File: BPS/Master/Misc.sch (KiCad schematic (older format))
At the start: 20 parts, among them J14 Conn_01x18, J3 FrontFans, J4 BackFans, Q6 BUT11

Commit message: Assigned footprints to all symbols except reset circuit(high voltage detector). Changed 18 pin connector to 3, 6 pin connectors. Generated netlist.
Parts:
- removed J14: Conn_01x18, symbol Connector_Generic:Conn_01x18
- added J12, J14, J15: Conn_01x06, UTSVT_Connectors:Molex_MicroFit_01x06_Horizontal, symbol Connector_Generic:Conn_01x06
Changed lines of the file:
@@
 Entry Wire Line
 	5300 4600 5400 4700
-$Comp
-L Connector_Generic:Conn_01x18 J14
-U 1 1 5F0A4204
-P 3700 6000
-F 0 "J14" V 3825 5946 50  0000 C CNN
-F 1 "Conn_01x18" V 3916 5946 50  0000 C CNN
-F 2 "" H 3700 6000 50  0001 C CNN
-F 3 "~" H 3700 6000 50  0001 C CNN
-	1    3700 6000
-	0    1    1    0
-$EndComp
 Wire Wire Line
 	2000 4700 2000 5800
@@
 Text Label 5400 4700 3    50   ~ 0
 IP17
+$Comp
+L Connector_Generic:Conn_01x06 J12
+U 1 1 5EF7E85A
+P 3100 6000
+F 0 "J12" V 3300 5950 50  0000 L CNN
+F 1 "Conn_01x06" V 3200 5750 50  0000 L CNN
+F 2 "UTSVT_Connectors:Molex_MicroFit_01x06_Horizontal" H 3100 6000 50  0001 C CNN
+F 3 "~" H 3100 6000 50  0001 C CNN
+	1    3100 6000
+	0    1    1    0
+$EndComp
+$Comp
+L Connector_Generic:Conn_01x06 J14
+U 1 1 5EF7ED81
+P 3700 6000
+F 0 "J14" V 3900 5900 50  0000 L CNN
+F 1 "Conn_01x06" V 3800 5750 50  0000 L CNN
+F 2 "UTSVT_Connectors:Molex_MicroFit_01x06_Horizontal" H 3700 6000 50  0001 C CNN
+F 3 "~" H 3700 6000 50  0001 C CNN
+	1    3700 6000
+	0    1    1    0
+$EndComp
+$Comp
+L Connector_Generic:Conn_01x06 J15
+U 1 1 5EF50D99
+P 4300 6000
+F 0 "J15" V 4500 5950 50  0000 L CNN
+F 1 "Conn_01x06" V 4400 5750 50  0000 L CNN
+F 2 "UTSVT_Connectors:Molex_MicroFit_01x06_Horizontal" H 4300 6000 50  0001 C CNN
+F 3 "~" H 4300 6000 50  0001 C CNN
+	1    4300 6000
+	0    1    1    0
+$EndComp
 Wire Bus Line
 	4350 1500 5450 1500

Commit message: Made file paths of symbol libraries relative. Added footprint for high voltage detection that is SMD and has same specs as one recommended in Bluetooth Module datasheet.
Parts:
- removed J12, J14, J15: Conn_01x06, UTSVT_Connectors:Molex_MicroFit_01x06_Horizontal, symbol Connector_Generic:Conn_01x06
- added J12, J14: Conn_01x08, UTSVT_Connectors:Molex_MicroFit3.0_2x4xP3.00mm_PolarizingPeg_Vertical, symbol Connector_Generic:Conn_01x08
- added J15: Conn_01x02, UTSVT_Connectors:Molex_MicroFit3.0_1x2xP3.00mm_PolarizingPeg_Vertical, symbol Connector_Generic:Conn_01x02
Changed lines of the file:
@@
 Text Label 5400 4700 3    50   ~ 0
 IP17
-$Comp
-L Connector_Generic:Conn_01x06 J12
-U 1 1 5EF7E85A
-P 3100 6000
-F 0 "J12" V 3300 5950 50  0000 L CNN
-F 1 "Conn_01x06" V 3200 5750 50  0000 L CNN
-F 2 "UTSVT_Connectors:Molex_MicroFit_01x06_Horizontal" H 3100 6000 50  0001 C CNN
-F 3 "~" H 3100 6000 50  0001 C CNN
-	1    3100 6000
-	0    1    1    0
-$EndComp
-$Comp
-L Connector_Generic:Conn_01x06 J14
-U 1 1 5EF7ED81
-P 3700 6000
-F 0 "J14" V 3900 5900 50  0000 L CNN
-F 1 "Conn_01x06" V 3800 5750 50  0000 L CNN
-F 2 "UTSVT_Connectors:Molex_MicroFit_01x06_Horizontal" H 3700 6000 50  0001 C CNN
-F 3 "~" H 3700 6000 50  0001 C CNN
-	1    3700 6000
-	0    1    1    0
-$EndComp
-$Comp
-L Connector_Generic:Conn_01x06 J15
-U 1 1 5EF50D99
-P 4300 6000
-F 0 "J15" V 4500 5950 50  0000 L CNN
-F 1 "Conn_01x06" V 4400 5750 50  0000 L CNN
-F 2 "UTSVT_Connectors:Molex_MicroFit_01x06_Horizontal" H 4300 6000 50  0001 C CNN
-F 3 "~" H 4300 6000 50  0001 C CNN
-	1    4300 6000
-	0    1    1    0
-$EndComp
 Wire Bus Line
 	4350 1500 5450 1500
@@
 Wire Bus Line
 	1800 4600 5500 4600
+$Comp
+L Connector_Generic:Conn_01x08 J12
+U 1 1 5EF670FD
+P 3200 6000
+F 0 "J12" V 3400 5950 50  0000 L CNN
+F 1 "Conn_01x08" V 3300 5750 50  0000 L CNN
+F 2 "UTSVT_Connectors:Molex_MicroFit3.0_2x4xP3.00mm_PolarizingPeg_Vertical" H 3200 6000 50  0001 C CNN
+F 3 "~" H 3200 6000 50  0001 C CNN
+	1    3200 6000
+	0    1    1    0
+$EndComp
+$Comp
+L Connector_Generic:Conn_01x08 J14
+U 1 1 5EF67B62
+P 4000 6000
+F 0 "J14" V 4200 5950 50  0000 L CNN
+F 1 "Conn_01x08" V 4100 5750 50  0000 L CNN
+F 2 "UTSVT_Connectors:Molex_MicroFit3.0_2x4xP3.00mm_PolarizingPeg_Vertical" H 4000 6000 50  0001 C CNN
+F 3 "~" H 4000 6000 50  0001 C CNN
+	1    4000 6000
+	0    1    1    0
+$EndComp
+$Comp
+L Connector_Generic:Conn_01x02 J15
+U 1 1 5EF68778
+P 4500 6000
+F 0 "J15" V 4700 5900 50  0000 L CNN
+F 1 "Conn_01x02" V 4600 5750 50  0000 L CNN
+F 2 "UTSVT_Connectors:Molex_MicroFit3.0_1x2xP3.00mm_PolarizingPeg_Vertical" H 4500 6000 50  0001 C CNN
+F 3 "~" H 4500 6000 50  0001 C CNN
+	1    4500 6000
+	0    1    1    0
+$EndComp
 $EndSCHEMATC

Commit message: Created new board for Bluetooth module because the antenna cannot have a ground plane on it. Made everything connect using pin headers. Will mount the Bluetooth module board onto the Master board.
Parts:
- removed J12, J14: Conn_01x08, UTSVT_Connectors:Molex_MicroFit3.0_2x4xP3.00mm_PolarizingPeg_Vertical, symbol Connector_Generic:Conn_01x08
- removed J15: Conn_01x02, UTSVT_Connectors:Molex_MicroFit3.0_1x2xP3.00mm_PolarizingPeg_Vertical, symbol Connector_Generic:Conn_01x02
- added J12, J14, J15: Conn_01x06, Connector_PinHeader_2.54mm:PinHeader_1x06_P2.54mm_Vertical, symbol Connector_Generic:Conn_01x06
- added J?: Conn_01x04, symbol Connector_Generic:Conn_01x04
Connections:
- net labels added: USART1_CTS, USART1_RTS, USART1_RX, USART1_TX
- net labels removed: +12V
- wire segments 114 -> 122
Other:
- note added: "For Bluetooth Module"
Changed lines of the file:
@@
 FANPWR
-$Comp
-L power:+12V #PWR0118
-U 1 1 5EE38D3D
-P 7000 1050
-F 0 "#PWR0118" H 7000 900 50  0001 C CNN
-F 1 "+12V" H 7015 1223 50  0000 C CNN
-F 2 "" H 7000 1050 50  0001 C CNN
-F 3 "" H 7000 1050 50  0001 C CNN
-	1    7000 1050
-	1    0    0    -1
-$EndComp
 $Comp
 L Transistor_BJT:BUT11 Q6
@@
 Text Label 5400 4700 3    50   ~ 0
 IP17
+$Comp
+L power:GND #PWR0108
+U 1 1 5EF8895A
+P 7000 1050
+F 0 "#PWR0108" H 7000 800 50  0001 C CNN
+F 1 "GND" H 7005 877 50  0000 C CNN
+F 2 "" H 7000 1050 50  0001 C CNN
+F 3 "" H 7000 1050 50  0001 C CNN
+	1    7000 1050
+	-1   0    0    1
+$EndComp
+$Comp
+L Connector_Generic:Conn_01x06 J12
+U 1 1 5EF8DB7E
+P 3100 6000
+F 0 "J12" V 3300 5950 50  0000 L CNN
+F 1 "Conn_01x06" V 3200 5750 50  0000 L CNN
+F 2 "Connector_PinHeader_2.54mm:PinHeader_1x06_P2.54mm_Vertical" H 3100 6000 50  0001 C CNN
+F 3 "~" H 3100 6000 50  0001 C CNN
+	1    3100 6000
+	0    1    1    0
+$EndComp
+$Comp
+L Connector_Generic:Conn_01x06 J14
+U 1 1 5EF8E106
+P 3700 6000
+F 0 "J14" V 3900 5950 50  0000 L CNN
+F 1 "Conn_01x06" V 3800 5750 50  0000 L CNN
+F 2 "Connector_PinHeader_2.54mm:PinHeader_1x06_P2.54mm_Vertical" H 3700 6000 50  0001 C CNN
+F 3 "~" H 3700 6000 50  0001 C CNN
+	1    3700 6000
+	0    1    1    0
+$EndComp
+$Comp
+L Connector_Generic:Conn_01x06 J15
+U 1 1 5EF8EC17
+P 4300 6000
+F 0 "J15" V 4500 5950 50  0000 L CNN
+F 1 "Conn_01x06" V 4400 5750 50  0000 L CNN
+F 2 "Connector_PinHeader_2.54mm:PinHeader_1x06_P2.54mm_Vertical" H 4300 6000 50  0001 C CNN
+F 3 "~" H 4300 6000 50  0001 C CNN
+	1    4300 6000
+	0    1    1    0
+$EndComp
+Entry Wire Line
+	5500 4600 5600 4700
+Entry Wire Line
+	5700 4600 5800 4700
+Entry Wire Line
+	5900 4600 6000 4700
+Entry Wire Line
+	6100 4600 6200 4700
+$Comp
+L Connector_Generic:Conn_01x04 J?
+U 1 1 5EFCE394
+P 5950 6000
+F 0 "J?" V 5822 6180 50  0000 L CNN
+F 1 "Conn_01x04" V 5913 6180 50  0000 L CNN
+F 2 "" H 5950 6000 50  0001 C CNN
+F 3 "~" H 5950 6000 50  0001 C CNN
+	1    5950 6000
+	0    1    1    0
+$EndComp
+Text Notes 5500 6200 0    50   ~ 0
+For Bluetooth Module
+Wire Wire Line
+	5600 4700 5600 5800
+Wire Wire Line
+	5600 5800 5750 5800
+Wire Wire Line
+	5800 4700 5800 5800
+Wire Wire Line
+	5800 5800 5850 5800
+Wire Wire Line
+	6000 4700 6000 5800
+Wire Wire Line
+	6000 5800 5950 5800
+Wire Wire Line
+	6200 4700 6200 5800
+Wire Wire Line
+	6200 5800 6050 5800
 Wire Bus Line
 	4350 1500 5450 1500
@@
 	1050 1500 3750 1500
 Wire Bus Line
-	1800 4600 5500 4600
-$Comp
-L Connector_Generic:Conn_01x08 J12
-U 1 1 5EF670FD
-P 3200 6000
-F 0 "J12" V 3400 5950 50  0000 L CNN
-F 1 "Conn_01x08" V 3300 5750 50  0000 L CNN
-F 2 "UTSVT_Connectors:Molex_MicroFit3.0_2x4xP3.00mm_PolarizingPeg_Vertical" H 3200 6000 50  0001 C CNN
-F 3 "~" H 3200 6000 50  0001 C CNN
-	1    3200 6000
-	0    1    1    0
-$EndComp
-$Comp
-L Connector_Generic:Conn_01x08 J14
-U 1 1 5EF67B62
-P 4000 6000
-F 0 "J14" V 4200 5950 50  0000 L CNN
-F 1 "Conn_01x08" V 4100 5750 50  0000 L CNN
-F 2 "UTSVT_Connectors:Molex_MicroFit3.0_2x4xP3.00mm_PolarizingPeg_Vertical" H 4000 6000 50  0001 C CNN
-F 3 "~" H 4000 6000 50  0001 C CNN
-	1    4000 6000
-	0    1    1    0
-$EndComp
-$Comp
-L Connector_Generic:Conn_01x02 J15
-U 1 1 5EF68778
-P 4500 6000
-F 0 "J15" V 4700 5900 50  0000 L CNN
-F 1 "Conn_01x02" V 4600 5750 50  0000 L CNN
-F 2 "UTSVT_Connectors:Molex_MicroFit3.0_1x2xP3.00mm_PolarizingPeg_Vertical" H 4500 6000 50  0001 C CNN
-F 3 "~" H 4500 6000 50  0001 C CNN
-	1    4500 6000
-	0    1    1    0
-$EndComp
+	1800 4600 6300 4600
+Text Label 5600 4700 3    50   ~ 0
+USART1_TX
+Text Label 5800 4700 3    50   ~ 0
+USART1_RX
+Text Label 6000 4700 3    50   ~ 0
+USART1_CTS
+Text Label 6200 4700 3    50   ~ 0
+USART1_RTS
 $EndSCHEMATC

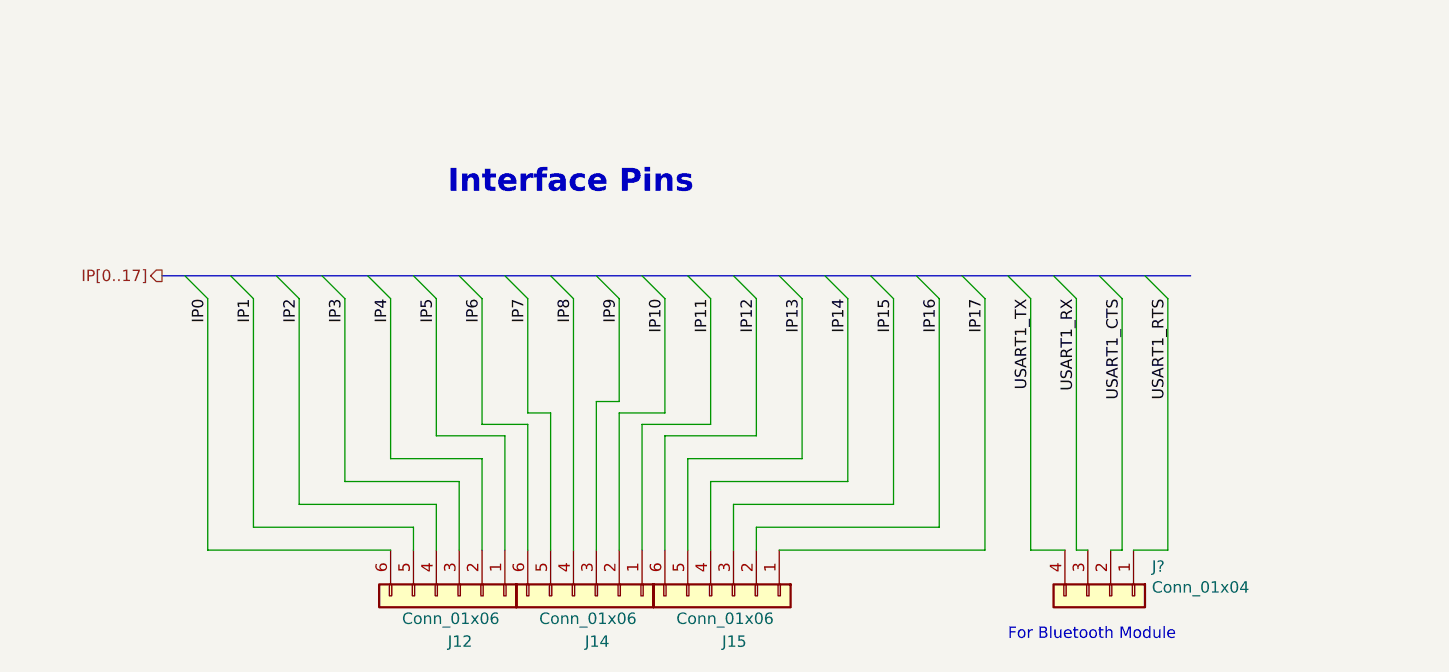
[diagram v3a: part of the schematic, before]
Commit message: Finished adding interface pins to master board. For some reason, the mosfet track isn't letting me connect to the fan power. I'm not sure why all these schematics are listed as modified because I didn't change anything in them.
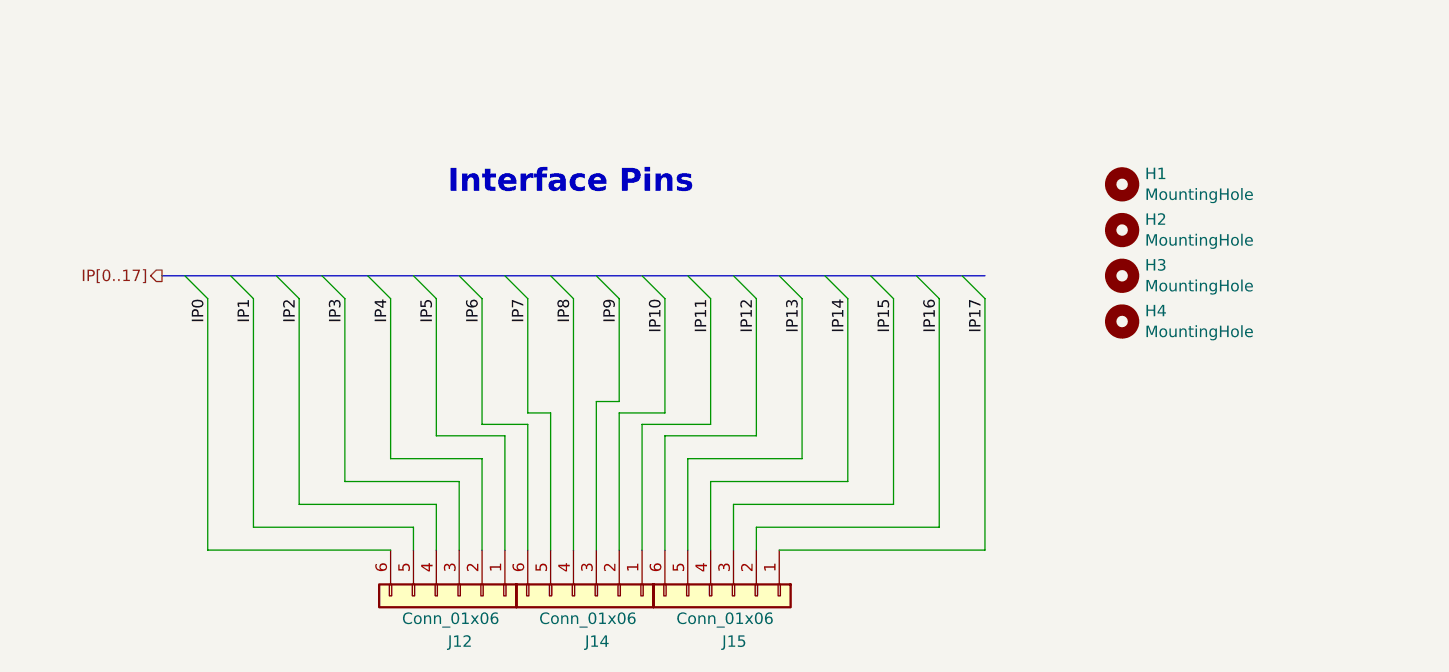
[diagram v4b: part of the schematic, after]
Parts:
- removed J?: Conn_01x04, symbol Connector_Generic:Conn_01x04
- added H1, H2, H3, H4: MountingHole, MountingHole:MountingHole_2.1mm, symbol Mechanical:MountingHole
- Q6: footprint Package_TO_SOT_THT:TO-220-3_Vertical -> Package_TO_SOT_SMD:SOT-23
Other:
- note removed: "For Bluetooth Module"
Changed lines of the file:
@@
 $Descr A4 11693 8268
 encoding utf-8
-Sheet 4 11
+Sheet 4 10
 Title ""
 Date ""
@@
 F 0 "Q6" H 7092 1296 50  0000 L CNN
 F 1 "BUT11" H 7092 1205 50  0000 L CNN
-F 2 "Package_TO_SOT_THT:TO-220-3_Vertical" H 7100 1175 50  0001 L CIN
+F 2 "Package_TO_SOT_SMD:SOT-23" H 7100 1175 50  0001 L CIN
 F 3 "http://www.fairchildsemi.com/ds/BU/BUT11.pdf" H 6900 1250 50  0001 L CNN
 	1    6900 1250
@@
 	0    1    1    0
 $EndComp
-Entry Wire Line
-	5500 4600 5600 4700
-Entry Wire Line
-	5700 4600 5800 4700
-Entry Wire Line
-	5900 4600 6000 4700
-Entry Wire Line
-	6100 4600 6200 4700
-$Comp
-L Connector_Generic:Conn_01x04 J?
-U 1 1 5EFCE394
-P 5950 6000
-F 0 "J?" V 5822 6180 50  0000 L CNN
-F 1 "Conn_01x04" V 5913 6180 50  0000 L CNN
-F 2 "" H 5950 6000 50  0001 C CNN
-F 3 "~" H 5950 6000 50  0001 C CNN
-	1    5950 6000
-	0    1    1    0
-$EndComp
-Text Notes 5500 6200 0    50   ~ 0
-For Bluetooth Module
-Wire Wire Line
-	5600 4700 5600 5800
-Wire Wire Line
-	5600 5800 5750 5800
-Wire Wire Line
-	5800 4700 5800 5800
-Wire Wire Line
-	5800 5800 5850 5800
-Wire Wire Line
-	6000 4700 6000 5800
-Wire Wire Line
-	6000 5800 5950 5800
-Wire Wire Line
-	6200 4700 6200 5800
-Wire Wire Line
-	6200 5800 6050 5800
+$Comp
+L Mechanical:MountingHole H?
+U 1 1 5F1A8D62
+P 6000 4800
+AR Path="/5F1A8D62" Ref="H?"  Part="1"
+AR Path="/5C392C6A/5F1A8D62" Ref="H4"  Part="1"
+F 0 "H4" H 6100 4846 50  0000 L CNN
+F 1 "MountingHole" H 6100 4755 50  0000 L CNN
+F 2 "MountingHole:MountingHole_2.1mm" H 6000 4800 50  0001 C CNN
+F 3 "~" H 6000 4800 50  0001 C CNN
+	1    6000 4800
+	1    0    0    -1
+$EndComp
+$Comp
+L Mechanical:MountingHole H?
+U 1 1 5F1A8D68
+P 6000 4600
+AR Path="/5F1A8D68" Ref="H?"  Part="1"
+AR Path="/5C392C6A/5F1A8D68" Ref="H3"  Part="1"
+F 0 "H3" H 6100 4646 50  0000 L CNN
+F 1 "MountingHole" H 6100 4555 50  0000 L CNN
+F 2 "MountingHole:MountingHole_2.1mm" H 6000 4600 50  0001 C CNN
+F 3 "~" H 6000 4600 50  0001 C CNN
+	1    6000 4600
+	1    0    0    -1
+$EndComp
+$Comp
+L Mechanical:MountingHole H?
+U 1 1 5F1A8D6E
+P 6000 4400
+AR Path="/5F1A8D6E" Ref="H?"  Part="1"
+AR Path="/5C392C6A/5F1A8D6E" Ref="H2"  Part="1"
+F 0 "H2" H 6100 4446 50  0000 L CNN
+F 1 "MountingHole" H 6100 4355 50  0000 L CNN
+F 2 "MountingHole:MountingHole_2.1mm" H 6000 4400 50  0001 C CNN
+F 3 "~" H 6000 4400 50  0001 C CNN
+	1    6000 4400
+	1    0    0    -1
+$EndComp
+$Comp
+L Mechanical:MountingHole H?
+U 1 1 5F1A8D74
+P 6000 4200
+AR Path="/5F1A8D74" Ref="H?"  Part="1"
+AR Path="/5C392C6A/5F1A8D74" Ref="H1"  Part="1"
+F 0 "H1" H 6100 4246 50  0000 L CNN
+F 1 "MountingHole" H 6100 4155 50  0000 L CNN
+F 2 "MountingHole:MountingHole_2.1mm" H 6000 4200 50  0001 C CNN
+F 3 "~" H 6000 4200 50  0001 C CNN
+	1    6000 4200
+	1    0    0    -1
+$EndComp
 Wire Bus Line
 	4350 1500 5450 1500
@@
 	1050 1500 3750 1500
 Wire Bus Line
-	1800 4600 6300 4600
-Text Label 5600 4700 3    50   ~ 0
-USART1_TX
-Text Label 5800 4700 3    50   ~ 0
-USART1_RX
-Text Label 6000 4700 3    50   ~ 0
-USART1_CTS
-Text Label 6200 4700 3    50   ~ 0
-USART1_RTS
+	1800 4600 5400 4600
 $EndSCHEMATC

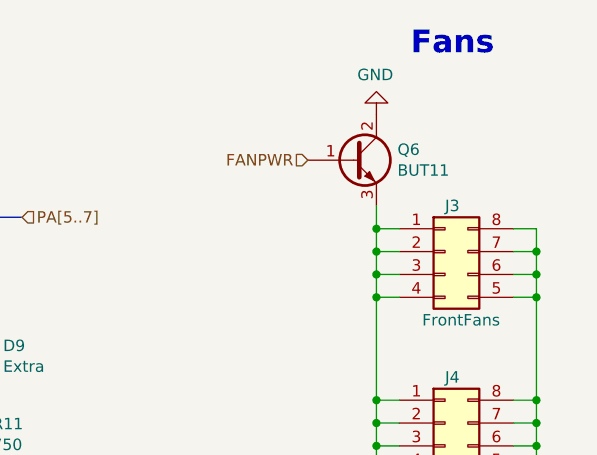
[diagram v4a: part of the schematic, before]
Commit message: Finished master board. Working to make sure that bluetooth mount won't cover anything important on master board, yet still be big enough to hold everything.
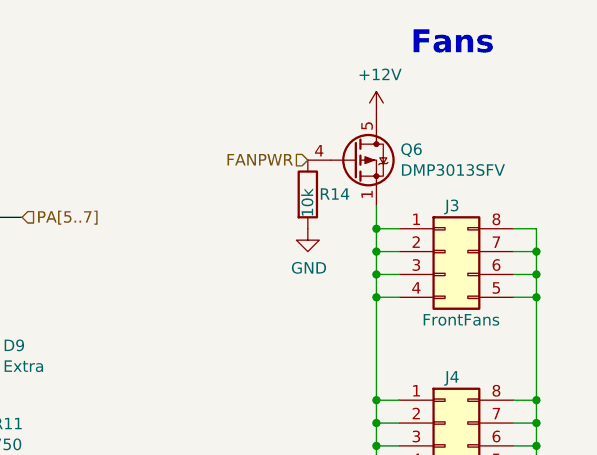
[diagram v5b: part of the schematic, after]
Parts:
- removed Q6: BUT11, Package_TO_SOT_SMD:SOT-23, symbol Transistor_BJT:BUT11
- added Q6: DMP3013SFV, Package_SON:Diodes_PowerDI3333-8, symbol Transistor_FET:DMP3013SFV
- added R14: 10k, Resistor_SMD:R_0805_2012Metric, symbol Device:R
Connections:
- net FANPWR: now also Q6.4 (G), R14.1
- net GND: now also R14.2
- net at J3.1 (Pin_1), J3.2 (Pin_2), J3.3 (Pin_3)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: now also Q6.1 (S), Q6.2 (S), Q6.3 (S)
- new net +12V: Q6.5 (D)
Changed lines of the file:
@@
 $EndComp
-Wire Wire Line
-	7000 1450 7000 1550
 Wire Wire Line
 	7000 1650 7100 1650
@@
 Connection ~ 7000 2500
 $Comp
-L power:GNDPWR #PWR030
-U 1 1 5C82C789
-P 7700 2700
-F 0 "#PWR030" H 7700 2500 50  0001 C CNN
-F 1 "GNDPWR" H 7704 2546 50  0000 C CNN
-F 2 "" H 7700 2650 50  0001 C CNN
-F 3 "" H 7700 2650 50  0001 C CNN
-	1    7700 2700
-	1    0    0    -1
-$EndComp
-$Comp
 L Device:LED_ALT D9
 U 1 1 5C585DBB
@@
 RUN
 Connection ~ 4750 2700
-Text HLabel 6700 1250 0    50   Input ~ 0
-FANPWR
-$Comp
-L Transistor_BJT:BUT11 Q6
-U 1 1 5EE3EB2A
-P 6900 1250
-F 0 "Q6" H 7092 1296 50  0000 L CNN
-F 1 "BUT11" H 7092 1205 50  0000 L CNN
-F 2 "Package_TO_SOT_SMD:SOT-23" H 7100 1175 50  0001 L CIN
-F 3 "http://www.fairchildsemi.com/ds/BU/BUT11.pdf" H 6900 1250 50  0001 L CNN
-	1    6900 1250
-	1    0    0    -1
-$EndComp
 Text HLabel 1800 4600 0    50   Output ~ 0
 IP[0..17]
@@
 IP17
 $Comp
-L power:GND #PWR0108
-U 1 1 5EF8895A
-P 7000 1050
-F 0 "#PWR0108" H 7000 800 50  0001 C CNN
-F 1 "GND" H 7005 877 50  0000 C CNN
-F 2 "" H 7000 1050 50  0001 C CNN
-F 3 "" H 7000 1050 50  0001 C CNN
-	1    7000 1050
-	-1   0    0    1
-$EndComp
-$Comp
 L Connector_Generic:Conn_01x06 J12
 U 1 1 5EF8DB7E
@@
 	1    0    0    -1
 $EndComp
+Wire Wire Line
+	7000 1450 7000 1550
+$Comp
+L power:GNDPWR #PWR030
+U 1 1 5C82C789
+P 7700 2700
+F 0 "#PWR030" H 7700 2500 50  0001 C CNN
+F 1 "GNDPWR" H 7704 2546 50  0000 C CNN
+F 2 "" H 7700 2650 50  0001 C CNN
+F 3 "" H 7700 2650 50  0001 C CNN
+	1    7700 2700
+	1    0    0    -1
+$EndComp
+Text HLabel 6700 1250 0    50   Input ~ 0
+FANPWR
+$Comp
+L power:+12V #PWR034
+U 1 1 5EFE2C60
+P 7000 1050
+F 0 "#PWR034" H 7000 900 50  0001 C CNN
+F 1 "+12V" H 7015 1223 50  0000 C CNN
+F 2 "" H 7000 1050 50  0001 C CNN
+F 3 "" H 7000 1050 50  0001 C CNN
+	1    7000 1050
+	1    0    0    -1
+$EndComp
+$Comp
+L Transistor_FET:DMP3013SFV Q6
+U 1 1 5EFE4C10
+P 6900 1250
+F 0 "Q6" H 7105 1296 50  0000 L CNN
+F 1 "DMP3013SFV" H 7105 1205 50  0000 L CNN
+F 2 "Package_SON:Diodes_PowerDI3333-8" H 7100 1175 50  0001 L CIN
+F 3 "https://www.diodes.com/assets/Datasheets/DMP3013SFV.pdf" V 6900 1250 50  0001 L CNN
+	1    6900 1250
+	1    0    0    -1
+$EndComp
+$Comp
+L Device:R R14
+U 1 1 5EFE4FE6
+P 6700 1400
+F 0 "R14" H 6750 1400 50  0000 L CNN
+F 1 "10k" V 6700 1300 50  0000 L CNN
+F 2 "Resistor_SMD:R_0805_2012Metric" V 6630 1400 50  0001 C CNN
+F 3 "~" H 6700 1400 50  0001 C CNN
+	1    6700 1400
+	1    0    0    -1
+$EndComp
+$Comp
+L power:GND #PWR035
+U 1 1 5EFE5415
+P 6700 1550
+F 0 "#PWR035" H 6700 1300 50  0001 C CNN
+F 1 "GND" H 6705 1377 50  0000 C CNN
+F 2 "" H 6700 1550 50  0001 C CNN
+F 3 "" H 6700 1550 50  0001 C CNN
+	1    6700 1550
+	1    0    0    -1
+$EndComp
